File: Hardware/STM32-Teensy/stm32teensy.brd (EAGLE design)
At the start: 160 x 100 mm, 25 parts, among them U1 STM32F413CGU3, U2 AP2112K-3.3TRG1, Y1 CRYSTAL-3.2X2.54-PIN

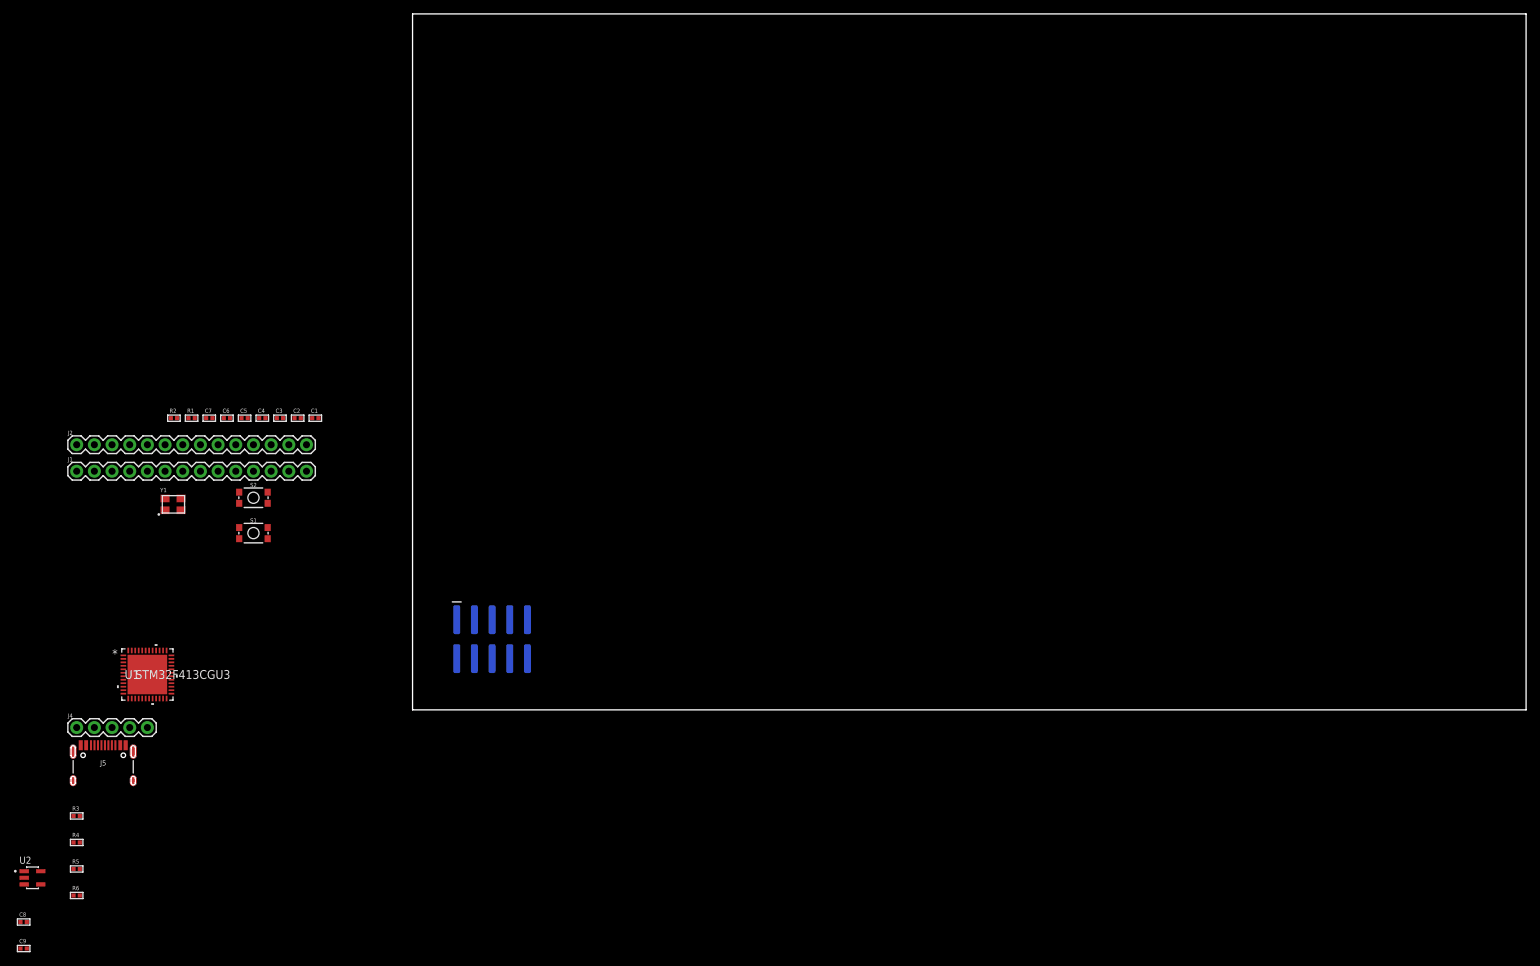
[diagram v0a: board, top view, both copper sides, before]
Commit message: ibooster v2, stm32teensy work
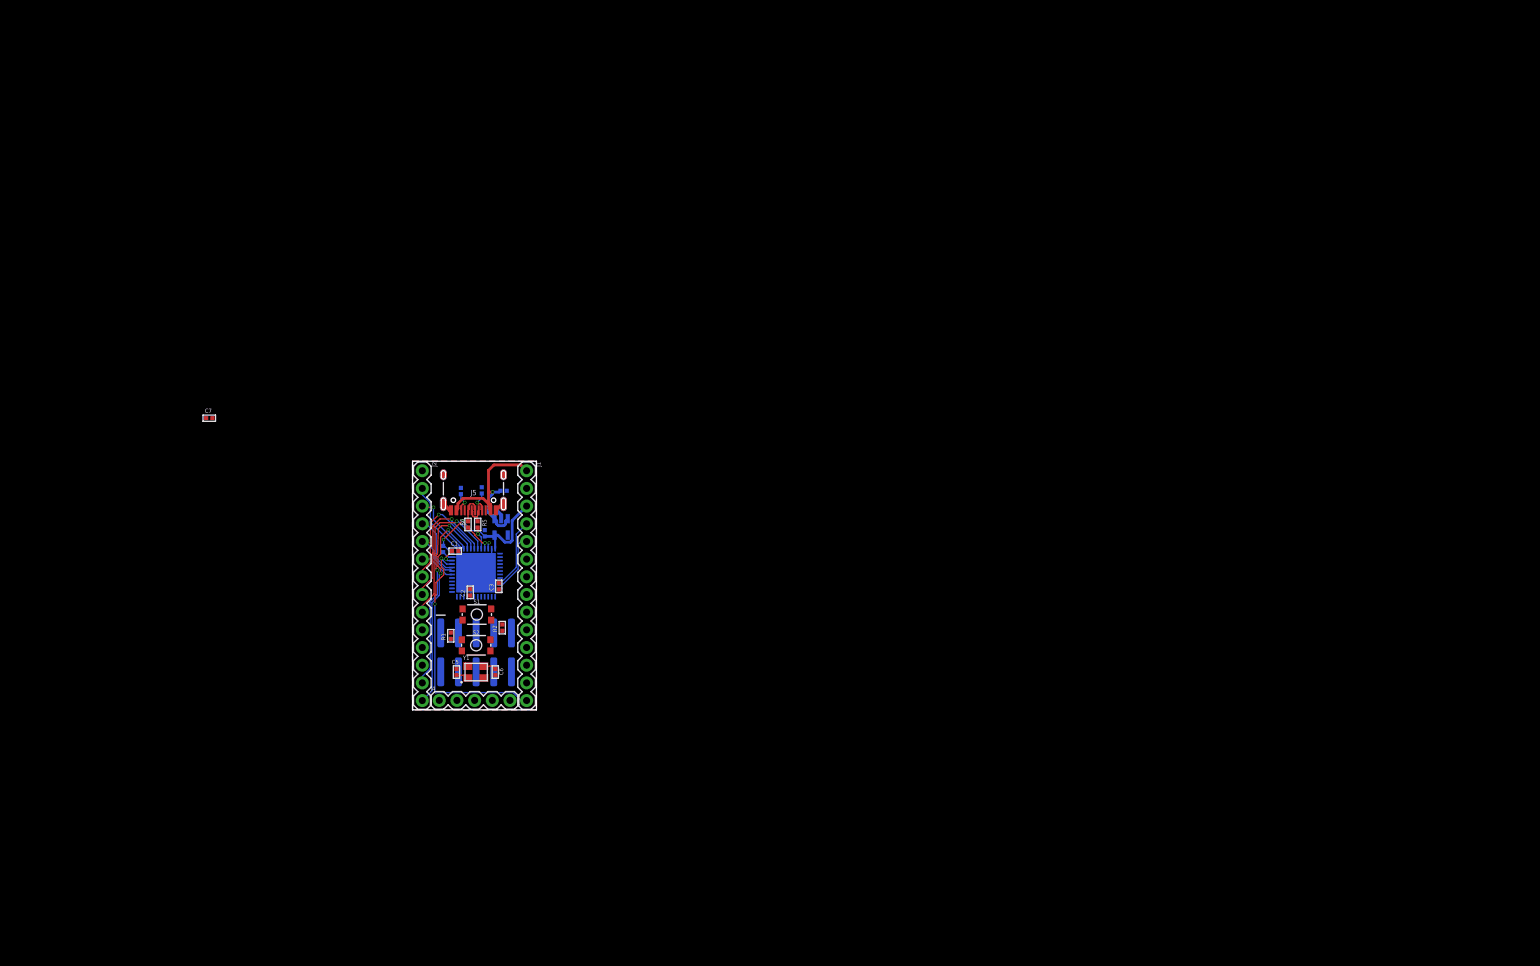
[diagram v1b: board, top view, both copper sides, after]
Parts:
- moved C8 92.7 mm to (13.1, 31.5), flipped to the bottom, turned to 180 degrees
- moved C9 89.2 mm to (10.4, 25.4), flipped to the bottom, turned to 90 degrees
- moved U2 84.1 mm to (12.7, 26.3), flipped to the bottom, turned to 270 degrees
- moved R6 77.5 mm to (7.97, 26.6), turned to 270 degrees
- moved R5 76.0 mm to (9.36, 26.6), turned to 270 degrees
- moved R4 74.8 mm to (6.95, 31.4), flipped to the bottom, turned to 270 degrees
- moved R3 74.7 mm to (9.94, 31.5), flipped to the bottom, turned to 270 degrees
- moved J1 64.7 mm to (16.4, 34.4), turned to 270 degrees
- moved J5 63.0 mm to (8.75, 28.7), turned to 180 degrees
- moved R2 56.0 mm to (12.9, 11.8), turned to 90 degrees
- moved C6 53.1 mm to (11.9, 5.43), turned to 90 degrees
- moved J4 52.2 mm to (3.84, 1.36)
- moved J2 49.8 mm to (1.40, 34.4), turned to 270 degrees
- moved Y1 49.7 mm to (7.94, 6.38)
- moved U1 49.4 mm to (9.12, 19.7), flipped to the bottom, turned to 90 degrees
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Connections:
- net GND: now also R3.1, R4.1
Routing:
- net PB10: track 0.00 -> 35.5 mm, vias 0 -> 2
- net PB14: track 0.00 -> 30.1 mm, vias 0 -> 2
- net PB15: track 0.00 -> 29.4 mm, vias 0 -> 2
- net 5V: track 0.00 -> 28.6 mm, vias 0 -> 1
- net 3.3V: track 0.00 -> 23.1 mm, vias 0 -> 2
- net N$21: track 0.00 -> 21.7 mm, vias 0 -> 1
- net N$20: track 0.00 -> 19.2 mm, vias 0 -> 1
- net GND: track 0.00 -> 18.6 mm
- net N$19: track 0.00 -> 17.0 mm, vias 0 -> 1
- net N$15: track 0.00 -> 10.7 mm
- net PB8: track 0.00 -> 10.1 mm
- net N$16: track 0.00 -> 9.23 mm, vias 0 -> 1
- net PB2: track 0.00 -> 8.92 mm
- net PB9: track 0.00 -> 8.49 mm
- net PB1: track 0.00 -> 6.73 mm
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- added copper zone on layer 1, net GND
- added copper zone on layer 16, net GND
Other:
- board size 160 x 100 mm -> 17.8 x 35.7 mm

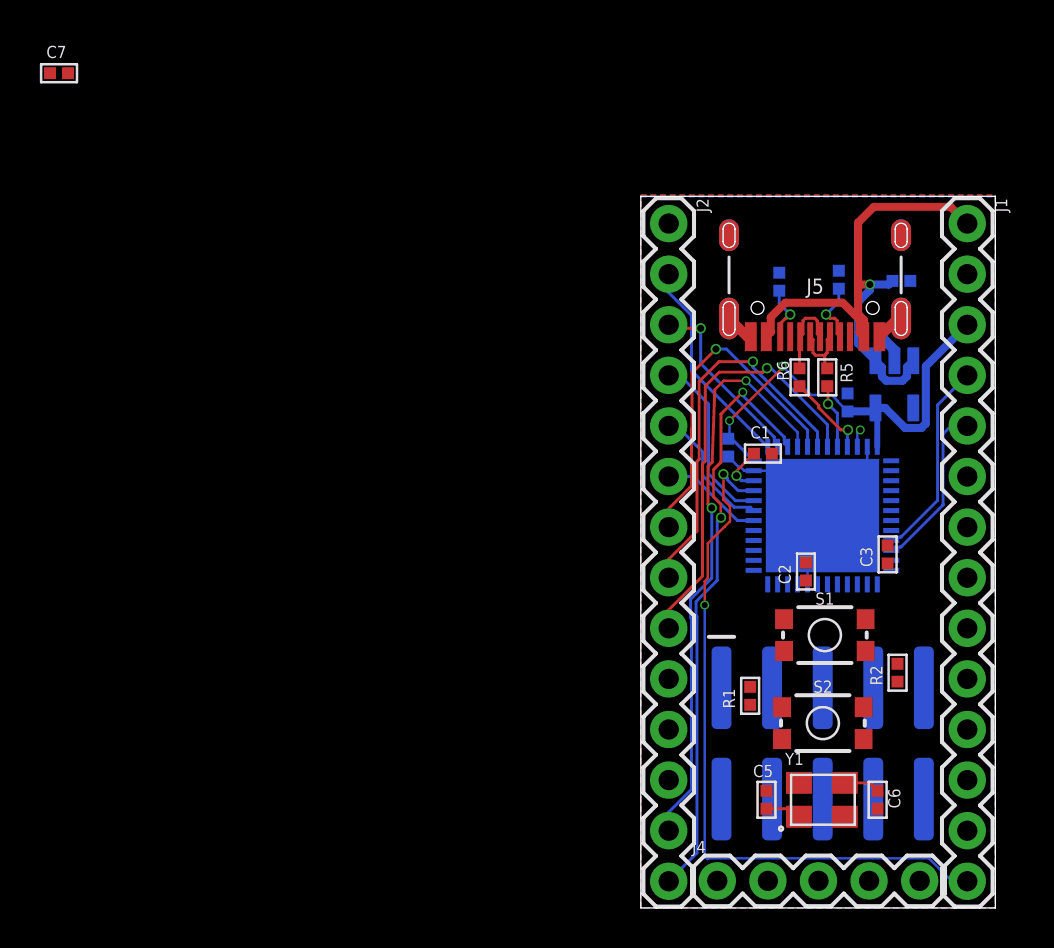
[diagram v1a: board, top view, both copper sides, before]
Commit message: stm32 teensy board
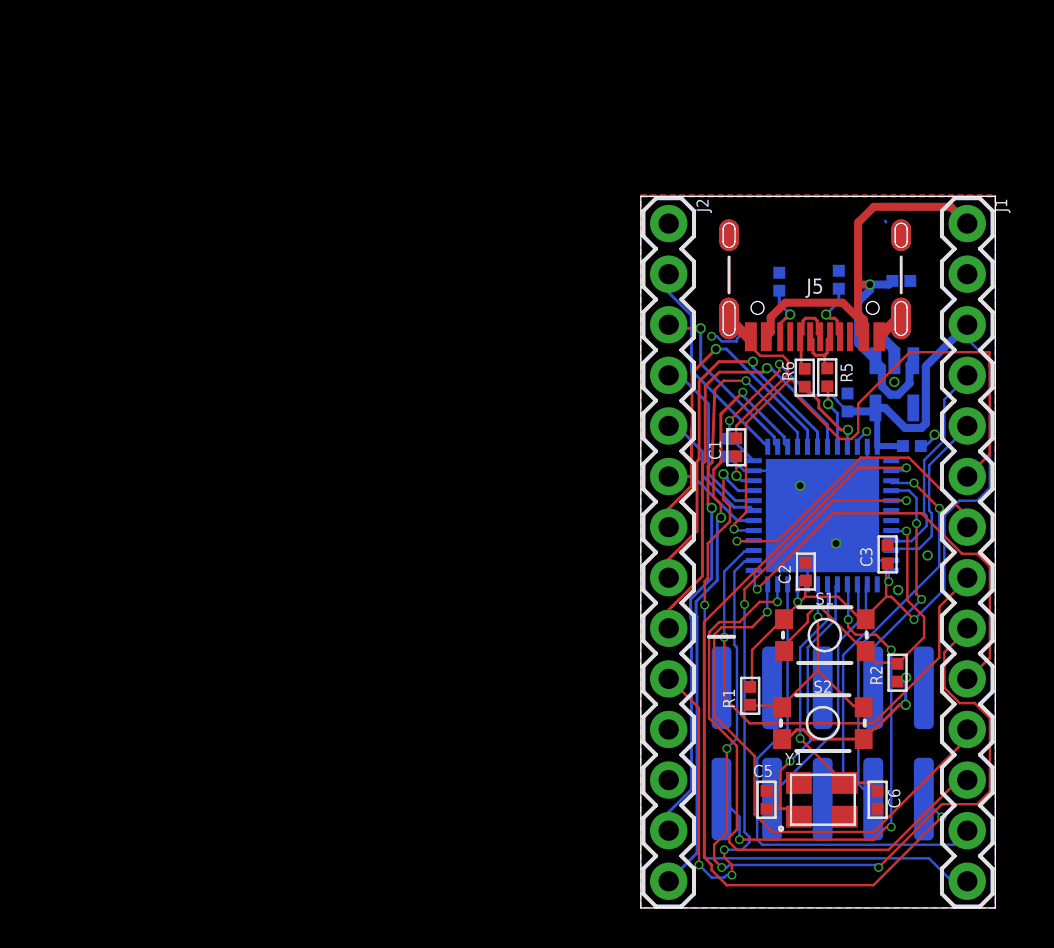
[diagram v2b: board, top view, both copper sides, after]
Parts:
- removed J4: (no value), SparkFun-Connectors:1X05
- moved C7 46.7 mm to (13.6, 23.2), flipped to the bottom, turned to 180 degrees
- moved C1 1.38 mm to (4.79, 23.1), turned to 90 degrees
- moved R6 0.26 mm to (8.23, 26.6)
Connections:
- net 3.3V: no longer J4.1
- net GND: no longer J4.5
- net NRST: no longer J4.4
- net SWC: no longer J4.3
- net SWD: no longer J4.2
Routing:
- net N$11: track 0.00 -> 41.9 mm, vias 0 -> 3
- net PA15: track 0.00 -> 41.4 mm, vias 0 -> 2
- net N$6: track 0.00 -> 38.4 mm, vias 0 -> 5
- net 3.3V: track 23.1 -> 59.1 mm, vias 2 -> 5
- net N$14: track 0.00 -> 30.7 mm, vias 0 -> 1
- net N$8: track 0.00 -> 29.8 mm, vias 0 -> 1
- net N$9: track 0.00 -> 27.8 mm, vias 0 -> 1
- net GND: track 18.6 -> 44.8 mm, vias 0 -> 9
- net N$12: track 0.00 -> 25.5 mm, vias 0 -> 1
- net N$5: track 0.00 -> 24.4 mm
- net N$23: track 0.00 -> 24.0 mm, vias 0 -> 4
- net N$10: track 0.00 -> 21.5 mm, vias 0 -> 1
- net PB3: track 0.00 -> 19.6 mm, vias 0 -> 2
- net N$2: track 0.00 -> 16.6 mm, vias 0 -> 1
- net N$13: track 0.00 -> 15.9 mm, vias 0 -> 1
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
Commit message: updates
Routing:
- net SWC: track 0.00 -> 1.34 mm, vias 0 -> 1
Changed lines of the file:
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@@
 <wire x1="4.826" y1="18.415" x2="5.588" y2="18.415" width="0.127" layer="16"/>
 <wire x1="6.858" y1="18.415" x2="4.826" y2="18.415" width="0.127" layer="1"/>
-<wire x1="11.049" y1="22.606" x2="6.858" y2="18.415" width="0.127" layer="1"/>
-<wire x1="13.462" y1="22.606" x2="11.049" y2="22.606" width="0.127" layer="1"/>
-<wire x1="16.383" y1="19.685" x2="13.462" y2="22.606" width="0.127" layer="1"/>
-<wire x1="16.383" y1="19.177" x2="16.383" y2="19.685" width="0.127" layer="1"/>
+<wire x1="10.749" y1="22.306" x2="6.858" y2="18.415" width="0.127" layer="1"/>
+<wire x1="13.472" y1="22.306" x2="10.749" y2="22.306" width="0.127" layer="1"/>
+<wire x1="16.383" y1="19.395" x2="13.472" y2="22.306" width="0.127" layer="1"/>
+<wire x1="16.383" y1="19.177" x2="16.383" y2="19.395" width="0.127" layer="1"/>
 <wire x1="5.588" y1="18.415" x2="5.668" y2="18.449684375" width="0.127" layer="16"/>
 <wire x1="16.383" y1="19.177" x2="16.39" y2="19.12" width="0.127" layer="1"/>
@@
 <signal name="SWC">
 <contactref element="U1" pad="37"/>
+<wire x1="12.572" y1="22.45069375" x2="13.82299375" y2="22.45069375" width="0.15" layer="16"/>
+<wire x1="13.82299375" y1="22.45069375" x2="13.88615" y2="22.51385" width="0.15" layer="16"/>
+<via x="13.88615" y="22.51385" extent="1-16" drill="0.3048"/>
 </signal>
 <signal name="PB8">
@@
 <wire x1="14.351" y1="19.177" x2="13.589" y2="18.415" width="0.127" layer="16"/>
 <wire x1="14.351" y1="19.685" x2="14.351" y2="19.177" width="0.127" layer="16"/>
-<wire x1="14.224" y1="19.812" x2="14.351" y2="19.685" width="0.127" layer="16"/>
-<wire x1="14.224" y1="22.479" x2="14.224" y2="19.812" width="0.127" layer="16"/>
-<wire x1="15.24" y1="23.495" x2="14.224" y2="22.479" width="0.127" layer="16"/>
-<wire x1="15.24" y1="25.527" x2="15.24" y2="23.495" width="0.127" layer="16"/>
+<wire x1="14.294" y1="19.742" x2="14.351" y2="19.685" width="0.127" layer="16"/>
+<wire x1="14.294" y1="22.329" x2="14.294" y2="19.742" width="0.127" layer="16"/>
+<wire x1="15.24" y1="23.275" x2="14.294" y2="22.329" width="0.127" layer="16"/>
+<wire x1="15.24" y1="25.527" x2="15.24" y2="23.275" width="0.127" layer="16"/>
 <wire x1="16.383" y1="26.67" x2="15.24" y2="25.527" width="0.127" layer="16"/>
 <wire x1="12.573" y1="18.415" x2="12.572" y2="18.449684375" width="0.127" layer="16"/>
@@
 <wire x1="14.605" y1="18.669" x2="13.97" y2="18.034" width="0.127" layer="16"/>
 <wire x1="14.605" y1="19.812" x2="14.605" y2="18.669" width="0.127" layer="16"/>
-<wire x1="14.478" y1="19.939" x2="14.605" y2="19.812" width="0.127" layer="16"/>
-<wire x1="14.478" y1="22.225" x2="14.478" y2="19.939" width="0.127" layer="16"/>
-<wire x1="16.383" y1="24.13" x2="14.478" y2="22.225" width="0.127" layer="16"/>
+<wire x1="14.548" y1="19.869" x2="14.605" y2="19.812" width="0.127" layer="16"/>
+<wire x1="14.548" y1="22.185" x2="14.548" y2="19.869" width="0.127" layer="16"/>
+<wire x1="16.370778125" y1="24.007778125" x2="14.548" y2="22.185" width="0.127" layer="16"/>
 <wire x1="12.573" y1="18.034" x2="12.572" y2="17.949559375" width="0.127" layer="16"/>
-<wire x1="16.383" y1="24.13" x2="16.39" y2="24.2" width="0.127" layer="16"/>
+<wire x1="16.370778125" y1="24.007778125" x2="16.39" y2="24.2" width="0.127" layer="16"/>
 </signal>
 <signal name="5V">
@@
 <contactref element="U1" pad="39"/>
 <contactref element="J3" pad="8"/>
-<wire x1="13.716" y1="21.336" x2="12.573" y2="21.336" width="0.127" layer="16"/>
-<wire x1="14.986" y1="20.066" x2="13.716" y2="21.336" width="0.127" layer="1"/>
+<wire x1="13.866" y1="21.236" x2="13.736" y2="21.366" width="0.127" layer="16"/>
+<wire x1="13.736" y1="21.366" x2="12.584315625" y2="21.366" width="0.127" layer="16"/>
+<wire x1="14.986" y1="20.066" x2="14.986" y2="20.116" width="0.127" layer="1"/>
+<wire x1="14.986" y1="20.116" x2="13.866" y2="21.236" width="0.127" layer="1"/>
 <wire x1="14.986" y1="17.145" x2="14.986" y2="20.066" width="0.127" layer="16"/>
 <wire x1="10.922" y1="13.081" x2="14.986" y2="17.145" width="0.127" layer="16"/>
 <wire x1="10.922" y1="6.223" x2="10.922" y2="13.081" width="0.127" layer="16"/>
 <wire x1="11.557" y1="5.588" x2="10.922" y2="6.223" width="0.127" layer="16"/>
-<wire x1="12.573" y1="21.336" x2="12.572" y2="21.450440625" width="0.127" layer="16"/>
+<wire x1="12.584315625" y1="21.366" x2="12.583675" y2="21.438765625" width="0.127" layer="16"/>
+<wire x1="12.583675" y1="21.438765625" x2="12.572" y2="21.450440625" width="0.127" layer="16"/>
 <wire x1="11.557" y1="5.588" x2="11.67" y2="5.466" width="0.127" layer="16"/>
-<via x="13.716" y="21.336" extent="1-16" drill="0.3048"/>
+<via x="13.866" y="21.236" extent="1-16" drill="0.3048"/>
 <via x="14.986" y="20.066" extent="1-16" drill="0.3048"/>
 </signal>
@@
 <contactref element="U1" pad="38"/>
 <contactref element="J3" pad="10"/>
-<wire x1="13.208" y1="21.971" x2="12.573" y2="21.971" width="0.127" layer="16"/>
-<wire x1="13.335" y1="22.098" x2="13.208" y2="21.971" width="0.127" layer="16"/>
-<wire x1="10.922" y1="22.098" x2="13.335" y2="22.098" width="0.127" layer="1"/>
-<wire x1="3.175" y1="14.351" x2="10.922" y2="22.098" width="0.127" layer="1"/>
+<wire x1="13.192" y1="21.971" x2="12.573" y2="21.971" width="0.127" layer="16"/>
+<wire x1="13.375" y1="21.788" x2="13.192" y2="21.971" width="0.127" layer="16"/>
+<wire x1="10.612" y1="21.788" x2="13.375" y2="21.788" width="0.127" layer="1"/>
+<wire x1="3.175" y1="14.351" x2="10.612" y2="21.788" width="0.127" layer="1"/>
 <wire x1="3.175" y1="2.54" x2="3.175" y2="14.351" width="0.127" layer="1"/>
 <wire x1="3.556" y1="2.159" x2="3.175" y2="2.54" width="0.127" layer="1"/>
@@
 <wire x1="12.573" y1="21.971" x2="12.572" y2="21.950565625" width="0.127" layer="16"/>
 <wire x1="14.224" y1="5.461" x2="14.21" y2="5.466" width="0.127" layer="16"/>
-<via x="13.335" y="22.098" extent="1-16" drill="0.3048"/>
+<via x="13.375" y="21.788" extent="1-16" drill="0.3048"/>
 <via x="15.113" y="4.572" extent="1-16" drill="0.3048"/>
 </signal>

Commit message: Ibooster board updates
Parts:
- C5, C6: value (none) -> 22p
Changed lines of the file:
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@@
 <attribute name="NAME" x="3.628" y="23.745" size="0.6096" layer="26" rot="MR270"/>
 </element>
-<element name="C5" library="comma.ai" package="0402-C" value="" x="6.31" y="5.43" smashed="yes" rot="R270">
+<element name="C5" library="comma.ai" package="0402-C" value="22p" x="6.31" y="5.43" smashed="yes" rot="R270">
 <attribute name="NAME" x="5.635" y="6.572" size="0.6096" layer="25"/>
 </element>
-<element name="C6" library="comma.ai" package="0402-C" value="" x="11.89" y="5.43" smashed="yes" rot="R90">
+<element name="C6" library="comma.ai" package="0402-C" value="22p" x="11.89" y="5.43" smashed="yes" rot="R90">
 <attribute name="NAME" x="13.028" y="4.995" size="0.6096" layer="25" rot="R90"/>
 </element>
